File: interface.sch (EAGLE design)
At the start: 19 parts, among them U1 ISL3179EIBZ, U2 ATMEGA328P

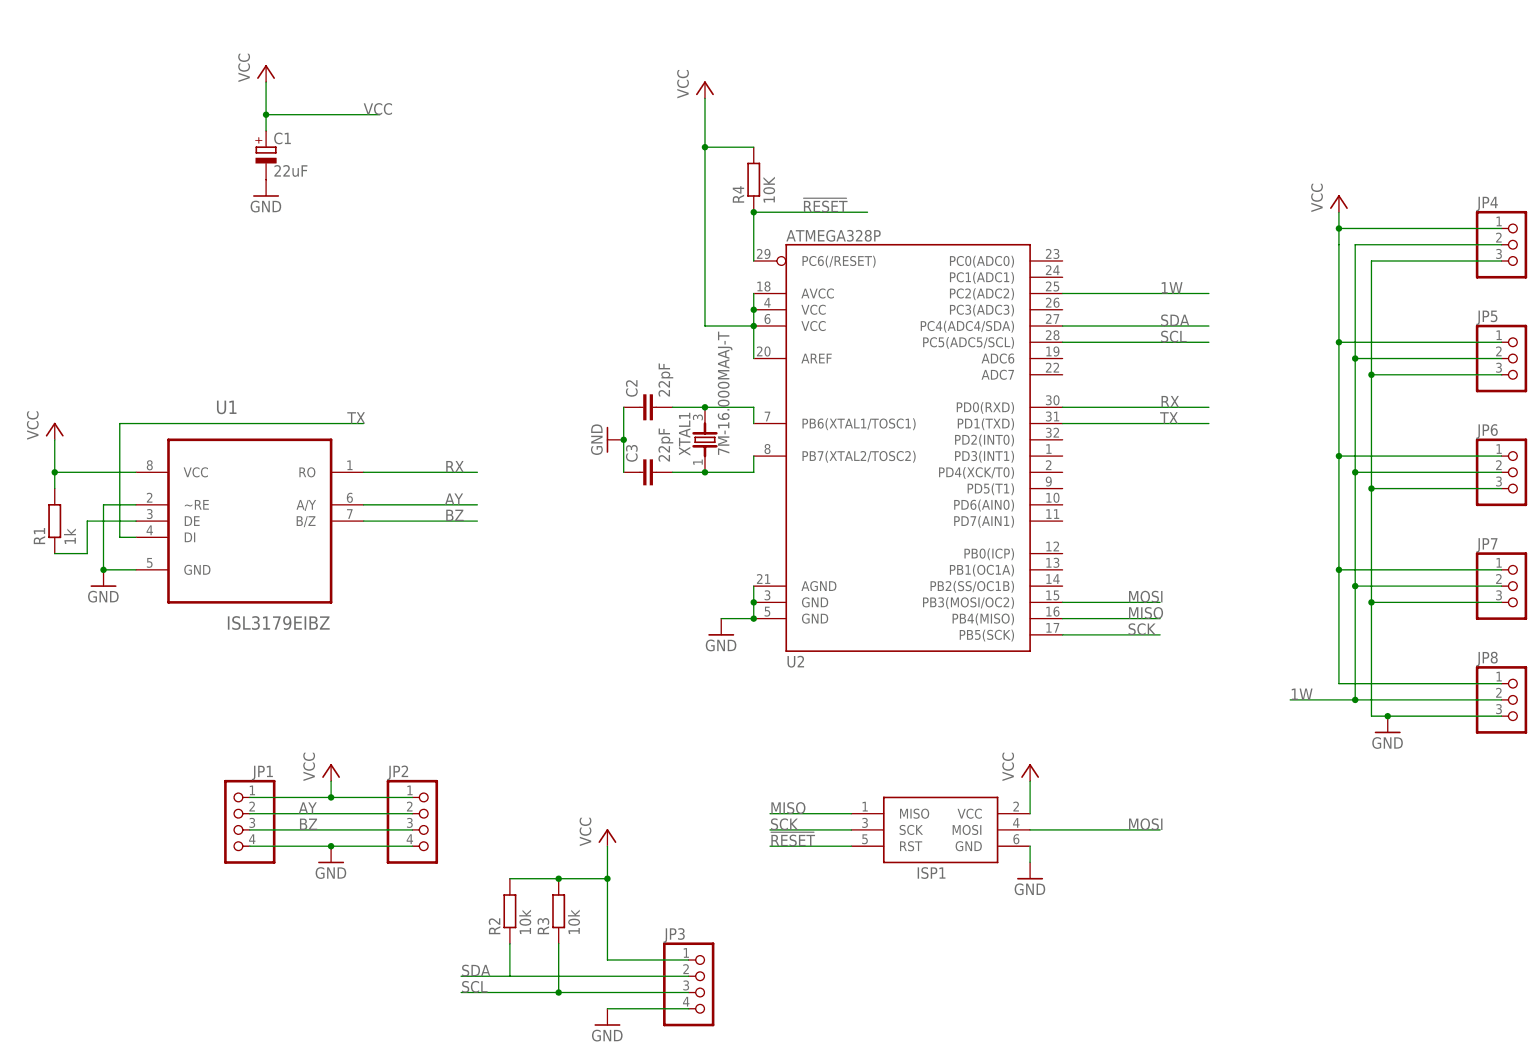
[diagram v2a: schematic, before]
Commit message: added optional 3v3 reg
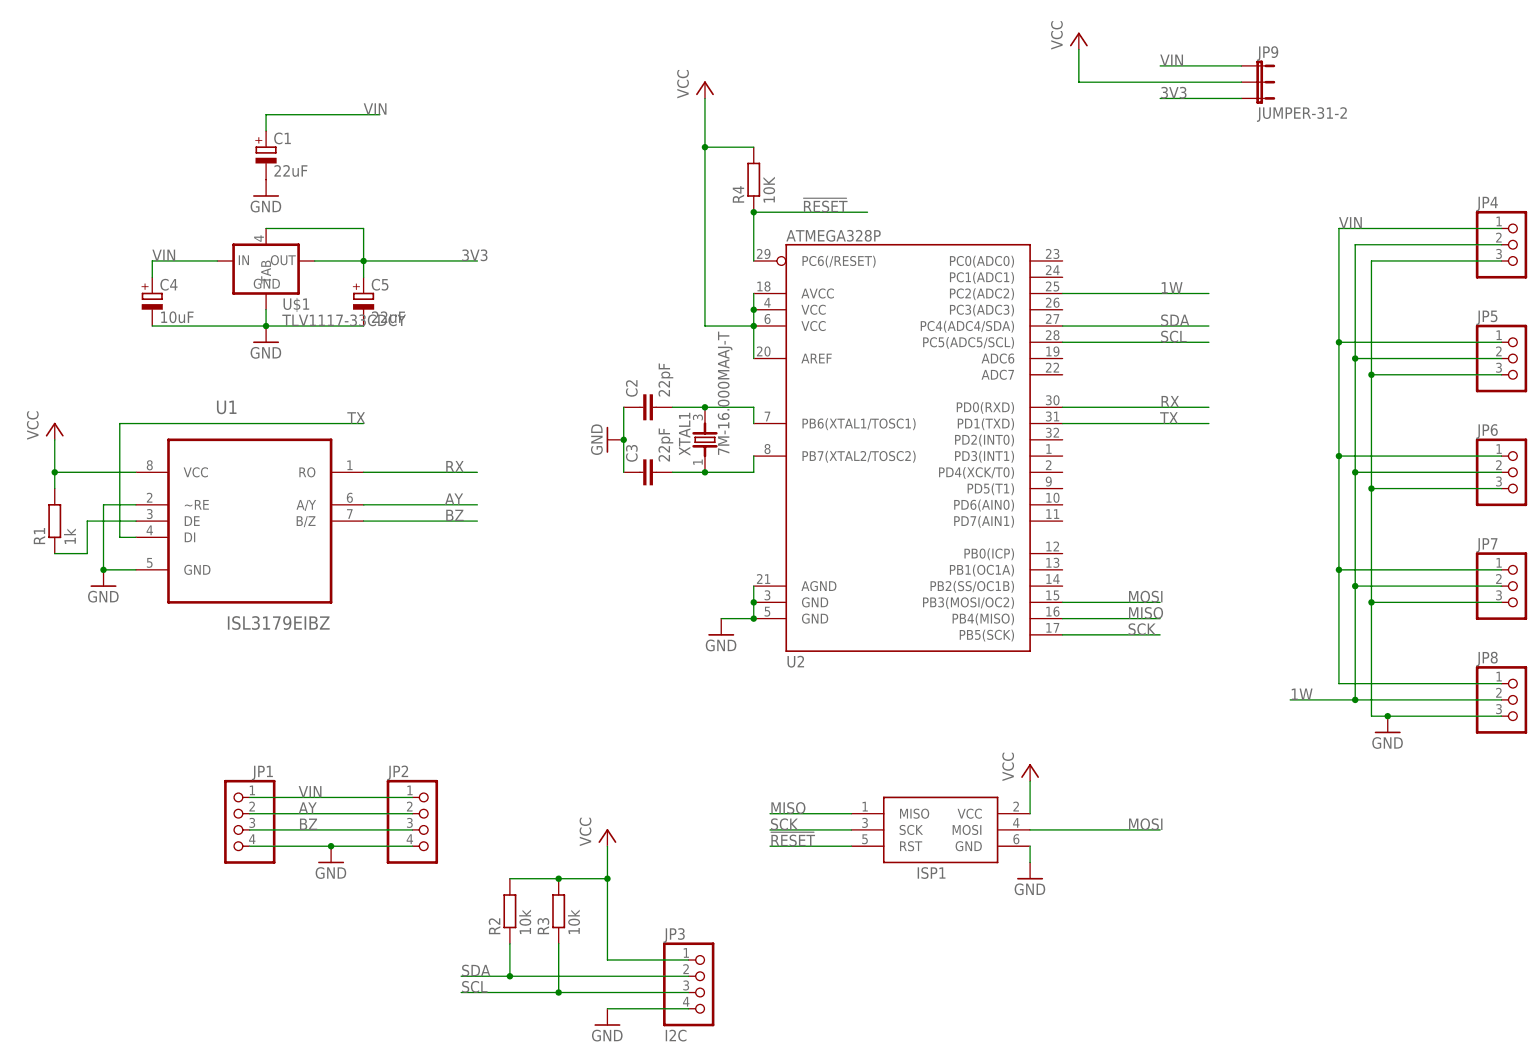
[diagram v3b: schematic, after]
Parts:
- added C4: 10uF, resistor:CPOL-EUA/3216-18R
- added C5: 22uF, resistor:CPOL-EUA/3216-18R
- added JP9: JUMPER-31-2, SparkFun-Passives:JUMPER-31-2
- added U$1: TLV1117-33CDCY, basestation:TLV1117-33CDCY
- JP3: value (none) -> I2C
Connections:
- new net 3V3: C5.+, JP9.3, U$1.OUT, U$1.TAB
- new net VIN: C1.+, C4.+, JP1.1, JP2.1, JP4.1, JP5.1, JP6.1, JP7.1, JP8.1, JP9.1, U$1.IN
- net GND: now also C4.-, C5.-, U$1.GND
- net VCC: now also JP9.2; no longer C1.+, JP1.1, JP2.1, JP4.1, JP5.1, JP6.1, JP7.1, JP8.1
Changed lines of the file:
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@@
 <part name="FRAME1" library="frames" deviceset="A4L-LOC" device=""/>
 <part name="U1" library="glacsweb" deviceset="ISL3179EIBZ" device=""/>
-<part name="P+1" library="glacsweb" deviceset="VCC" device=""/>
 <part name="C1" library="resistor" deviceset="CPOL-EU" device="A/3216-18R" value="22uF"/>
 <part name="GND3" library="supply1" deviceset="GND" device=""/>
@@
 <part name="JP1" library="pinhead" deviceset="PINHD-1X4" device=""/>
 <part name="GND6" library="supply1" deviceset="GND" device=""/>
-<part name="P+3" library="glacsweb" deviceset="VCC" device=""/>
 <part name="GND1" library="supply1" deviceset="GND" device=""/>
 <part name="P+4" library="glacsweb" deviceset="VCC" device=""/>
-<part name="JP3" library="pinhead" deviceset="PINHD-1X4" device=""/>
+<part name="JP3" library="pinhead" deviceset="PINHD-1X4" device="" value="I2C"/>
 <part name="GND2" library="supply1" deviceset="GND" device=""/>
 <part name="P+6" library="glacsweb" deviceset="VCC" device=""/>
@@
 <part name="JP8" library="pinhead" deviceset="PINHD-1X3" device=""/>
 <part name="GND7" library="supply1" deviceset="GND" device=""/>
-<part name="P+7" library="glacsweb" deviceset="VCC" device=""/>
 <part name="R3" library="resistor" deviceset="R-EU_" device="R0805" value="10k"/>
 <part name="R2" library="resistor" deviceset="R-EU_" device="R0805" value="10k"/>
@@
 <part name="GND4" library="supply1" deviceset="GND" device=""/>
 <part name="XTAL1" library="TXC-7M-16.000MAAJ-T" deviceset="7M-16.000MAAJ-T" device=""/>
+<part name="U$1" library="basestation" deviceset="TLV1117-33CDCY" device=""/>
+<part name="C4" library="resistor" deviceset="CPOL-EU" device="A/3216-18R" value="10uF"/>
+<part name="C5" library="resistor" deviceset="CPOL-EU" device="A/3216-18R" value="22uF"/>
+<part name="GND9" library="supply1" deviceset="GND" device=""/>
+<part name="JP9" library="SparkFun-Passives" deviceset="JUMPER-3" device="1-2"/>
+<part name="P+5" library="glacsweb" deviceset="VCC" device=""/>
 </parts>
 <sheets>
@@
 <instance part="FRAME1" gate="G$1" x="0" y="0"/>
 <instance part="U1" gate="A" x="43.18" y="93.98"/>
-<instance part="P+1" gate="VCC" x="45.72" y="162.56"/>
 <instance part="C1" gate="G$1" x="45.72" y="149.86"/>
 <instance part="GND3" gate="1" x="20.32" y="81.28"/>
@@
 <instance part="JP1" gate="A" x="40.64" y="43.18" rot="MR0"/>
 <instance part="GND6" gate="1" x="55.88" y="38.1"/>
-<instance part="P+3" gate="VCC" x="55.88" y="53.34"/>
 <instance part="GND1" gate="1" x="45.72" y="142.24"/>
 <instance part="P+4" gate="VCC" x="12.7" y="106.68"/>
@@
 <instance part="JP8" gate="A" x="241.3" y="63.5"/>
 <instance part="GND7" gate="1" x="220.98" y="58.42"/>
-<instance part="P+7" gate="VCC" x="213.36" y="142.24"/>
 <instance part="R3" gate="G$1" x="91.44" y="30.48" rot="R90"/>
 <instance part="R2" gate="G$1" x="83.82" y="30.48" rot="R90"/>
@@
 <instance part="GND4" gate="1" x="99.06" y="104.14" rot="R270"/>
 <instance part="XTAL1" gate="A" x="114.3" y="104.14" rot="R90"/>
+<instance part="U$1" gate="G$1" x="45.72" y="129.54"/>
+<instance part="C4" gate="G$1" x="27.94" y="127"/>
+<instance part="C5" gate="G$1" x="60.96" y="127"/>
+<instance part="GND9" gate="1" x="45.72" y="119.38"/>
+<instance part="JP9" gate="G$1" x="200.66" y="162.56" rot="R270"/>
+<instance part="P+5" gate="VCC" x="172.72" y="167.64"/>
 </instances>
 <busses>
@@
 <junction x="101.6" y="104.14"/>
 </segment>
+<segment>
+<pinref part="C4" gate="G$1" pin="-"/>
+<pinref part="U$1" gate="G$1" pin="GND"/>
+<wire x1="27.94" y1="121.92" x2="45.72" y2="121.92" width="0.1524" layer="91"/>
+<wire x1="45.72" y1="121.92" x2="45.72" y2="124.46" width="0.1524" layer="91"/>
+<pinref part="C5" gate="G$1" pin="-"/>
+<wire x1="60.96" y1="121.92" x2="45.72" y2="121.92" width="0.1524" layer="91"/>
+<junction x="45.72" y="121.92"/>
+<pinref part="GND9" gate="1" pin="GND"/>
+</segment>
 </net>
 <net name="VCC" class="0">
@@
 <pinref part="P+2" gate="VCC" pin="VCC"/>
 <wire x1="165.1" y1="45.72" x2="165.1" y2="50.8" width="0.1524" layer="91"/>
-</segment>
-<segment>
-<pinref part="JP1" gate="A" pin="1"/>
-<pinref part="JP2" gate="A" pin="1"/>
-<wire x1="43.18" y1="48.26" x2="55.88" y2="48.26" width="0.1524" layer="91"/>
-<pinref part="P+3" gate="VCC" pin="VCC"/>
-<wire x1="55.88" y1="48.26" x2="68.58" y2="48.26" width="0.1524" layer="91"/>
-<wire x1="55.88" y1="48.26" x2="55.88" y2="50.8" width="0.1524" layer="91"/>
-<junction x="55.88" y="48.26"/>
-</segment>
-<segment>
-<pinref part="C1" gate="G$1" pin="+"/>
-<wire x1="45.72" y1="152.4" x2="45.72" y2="154.94" width="0.1524" layer="91"/>
-<junction x="45.72" y="154.94"/>
-<wire x1="45.72" y1="160.02" x2="45.72" y2="154.94" width="0.1524" layer="91"/>
-<wire x1="45.72" y1="154.94" x2="63.5" y2="154.94" width="0.1524" layer="91"/>
-<label x="60.96" y="154.94" size="1.778" layer="95"/>
-<pinref part="P+1" gate="VCC" pin="VCC"/>
 </segment>
 <segment>
@@
 <wire x1="91.44" y1="35.56" x2="99.06" y2="35.56" width="0.1524" layer="91"/>
 <junction x="99.06" y="35.56"/>
-</segment>
-<segment>
-<pinref part="JP4" gate="A" pin="1"/>
-<wire x1="238.76" y1="137.16" x2="213.36" y2="137.16" width="0.1524" layer="91"/>
-<wire x1="213.36" y1="137.16" x2="213.36" y2="134.62" width="0.1524" layer="91"/>
-<pinref part="JP8" gate="A" pin="1"/>
-<wire x1="213.36" y1="134.62" x2="213.36" y2="119.38" width="0.1524" layer="91"/>
-<wire x1="213.36" y1="119.38" x2="213.36" y2="101.6" width="0.1524" layer="91"/>
-<wire x1="213.36" y1="101.6" x2="213.36" y2="83.82" width="0.1524" layer="91"/>
-<wire x1="213.36" y1="83.82" x2="213.36" y2="66.04" width="0.1524" layer="91"/>
-<wire x1="213.36" y1="66.04" x2="238.76" y2="66.04" width="0.1524" layer="91"/>
-<pinref part="JP5" gate="A" pin="1"/>
-<wire x1="238.76" y1="119.38" x2="213.36" y2="119.38" width="0.1524" layer="91"/>
-<pinref part="JP6" gate="A" pin="1"/>
-<wire x1="238.76" y1="101.6" x2="213.36" y2="101.6" width="0.1524" layer="91"/>
-<pinref part="JP7" gate="A" pin="1"/>
-<wire x1="238.76" y1="83.82" x2="213.36" y2="83.82" width="0.1524" layer="91"/>
-<junction x="213.36" y="119.38"/>
-<junction x="213.36" y="101.6"/>
-<junction x="213.36" y="83.82"/>
-<pinref part="P+7" gate="VCC" pin="VCC"/>
-<wire x1="213.36" y1="139.7" x2="213.36" y2="137.16" width="0.1524" layer="91"/>
-<junction x="213.36" y="137.16"/>
 </segment>
 <segment>
@@
 <junction x="114.3" y="149.86"/>
 </segment>
+<segment>
+<pinref part="JP9" gate="G$1" pin="2"/>
+<wire x1="198.12" y1="160.02" x2="172.72" y2="160.02" width="0.1524" layer="91"/>
+<wire x1="172.72" y1="160.02" x2="172.72" y2="165.1" width="0.1524" layer="91"/>
+<pinref part="P+5" gate="VCC" pin="VCC"/>
+</segment>
 </net>
 <net name="AY" class="0">
@@
 <wire x1="83.82" y1="20.32" x2="76.2" y2="20.32" width="0.1524" layer="91"/>
 <wire x1="83.82" y1="25.4" x2="83.82" y2="20.32" width="0.1524" layer="91"/>
+<junction x="83.82" y="20.32"/>
 </segment>
 <segment>
@@
 </segment>
 </net>
+<net name="3V3" class="0">
+<segment>
+<pinref part="U$1" gate="G$1" pin="OUT"/>
+<wire x1="53.34" y1="132.08" x2="60.96" y2="132.08" width="0.1524" layer="91"/>
+<pinref part="C5" gate="G$1" pin="+"/>
+<wire x1="60.96" y1="129.54" x2="60.96" y2="132.08" width="0.1524" layer="91"/>
+<junction x="60.96" y="132.08"/>
+<wire x1="60.96" y1="137.16" x2="60.96" y2="132.08" width="0.1524" layer="91"/>
+<pinref part="U$1" gate="G$1" pin="TAB"/>
+<wire x1="45.72" y1="137.16" x2="60.96" y2="137.16" width="0.1524" layer="91"/>
+<wire x1="60.96" y1="132.08" x2="78.74" y2="132.08" width="0.1524" layer="91"/>
+<label x="76.2" y="132.08" size="1.778" layer="95"/>
+</segment>
+<segment>
+<pinref part="JP9" gate="G$1" pin="3"/>
+<wire x1="198.12" y1="157.48" x2="185.42" y2="157.48" width="0.1524" layer="91"/>
+<label x="185.42" y="157.48" size="1.778" layer="95"/>
+</segment>
+</net>
+<net name="VIN" class="0">
+<segment>
+<pinref part="C1" gate="G$1" pin="+"/>
+<wire x1="45.72" y1="152.4" x2="45.72" y2="154.94" width="0.1524" layer="91"/>
+<wire x1="45.72" y1="154.94" x2="63.5" y2="154.94" width="0.1524" layer="91"/>
+<label x="60.96" y="154.94" size="1.778" layer="95"/>
+</segment>
+<segment>
+<pinref part="JP1" gate="A" pin="1"/>
+<pinref part="JP2" gate="A" pin="1"/>
+<wire x1="43.18" y1="48.26" x2="68.58" y2="48.26" width="0.1524" layer="91"/>
+<label x="50.8" y="48.26" size="1.778" layer="95"/>
+</segment>
+<segment>
+<pinref part="U$1" gate="G$1" pin="IN"/>
+<pinref part="C4" gate="G$1" pin="+"/>
+<wire x1="38.1" y1="132.08" x2="27.94" y2="132.08" width="0.1524" layer="91"/>
+<wire x1="27.94" y1="132.08" x2="27.94" y2="129.54" width="0.1524" layer="91"/>
+<label x="27.94" y="132.08" size="1.778" layer="95"/>
+</segment>
+<segment>
+<pinref part="JP9" gate="G$1" pin="1"/>
+<wire x1="198.12" y1="162.56" x2="185.42" y2="162.56" width="0.1524" layer="91"/>
+<label x="185.42" y="162.56" size="1.778" layer="95"/>
+</segment>
+<segment>
+<pinref part="JP4" gate="A" pin="1"/>
+<wire x1="238.76" y1="137.16" x2="213.36" y2="137.16" width="0.1524" layer="91"/>
+<pinref part="JP8" gate="A" pin="1"/>
+<wire x1="213.36" y1="137.16" x2="213.36" y2="119.38" width="0.1524" layer="91"/>
+<wire x1="213.36" y1="119.38" x2="213.36" y2="101.6" width="0.1524" layer="91"/>
+<wire x1="213.36" y1="101.6" x2="213.36" y2="83.82" width="0.1524" layer="91"/>
+<wire x1="213.36" y1="83.82" x2="213.36" y2="66.04" width="0.1524" layer="91"/>
+<wire x1="213.36" y1="66.04" x2="238.76" y2="66.04" width="0.1524" layer="91"/>
+<pinref part="JP5" gate="A" pin="1"/>
+<wire x1="238.76" y1="119.38" x2="213.36" y2="119.38" width="0.1524" layer="91"/>
+<pinref part="JP6" gate="A" pin="1"/>
+<wire x1="238.76" y1="101.6" x2="213.36" y2="101.6" width="0.1524" layer="91"/>
+<pinref part="JP7" gate="A" pin="1"/>
+<wire x1="238.76" y1="83.82" x2="213.36" y2="83.82" width="0.1524" layer="91"/>
+<junction x="213.36" y="119.38"/>
+<junction x="213.36" y="101.6"/>
+<junction x="213.36" y="83.82"/>
+<label x="213.36" y="137.16" size="1.778" layer="95"/>
+</segment>
+</net>
